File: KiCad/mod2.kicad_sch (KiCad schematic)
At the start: 47 parts, among them M3 Fan_4pin, M4 Fan_4pin, U2 ZD25Q64BSIGT

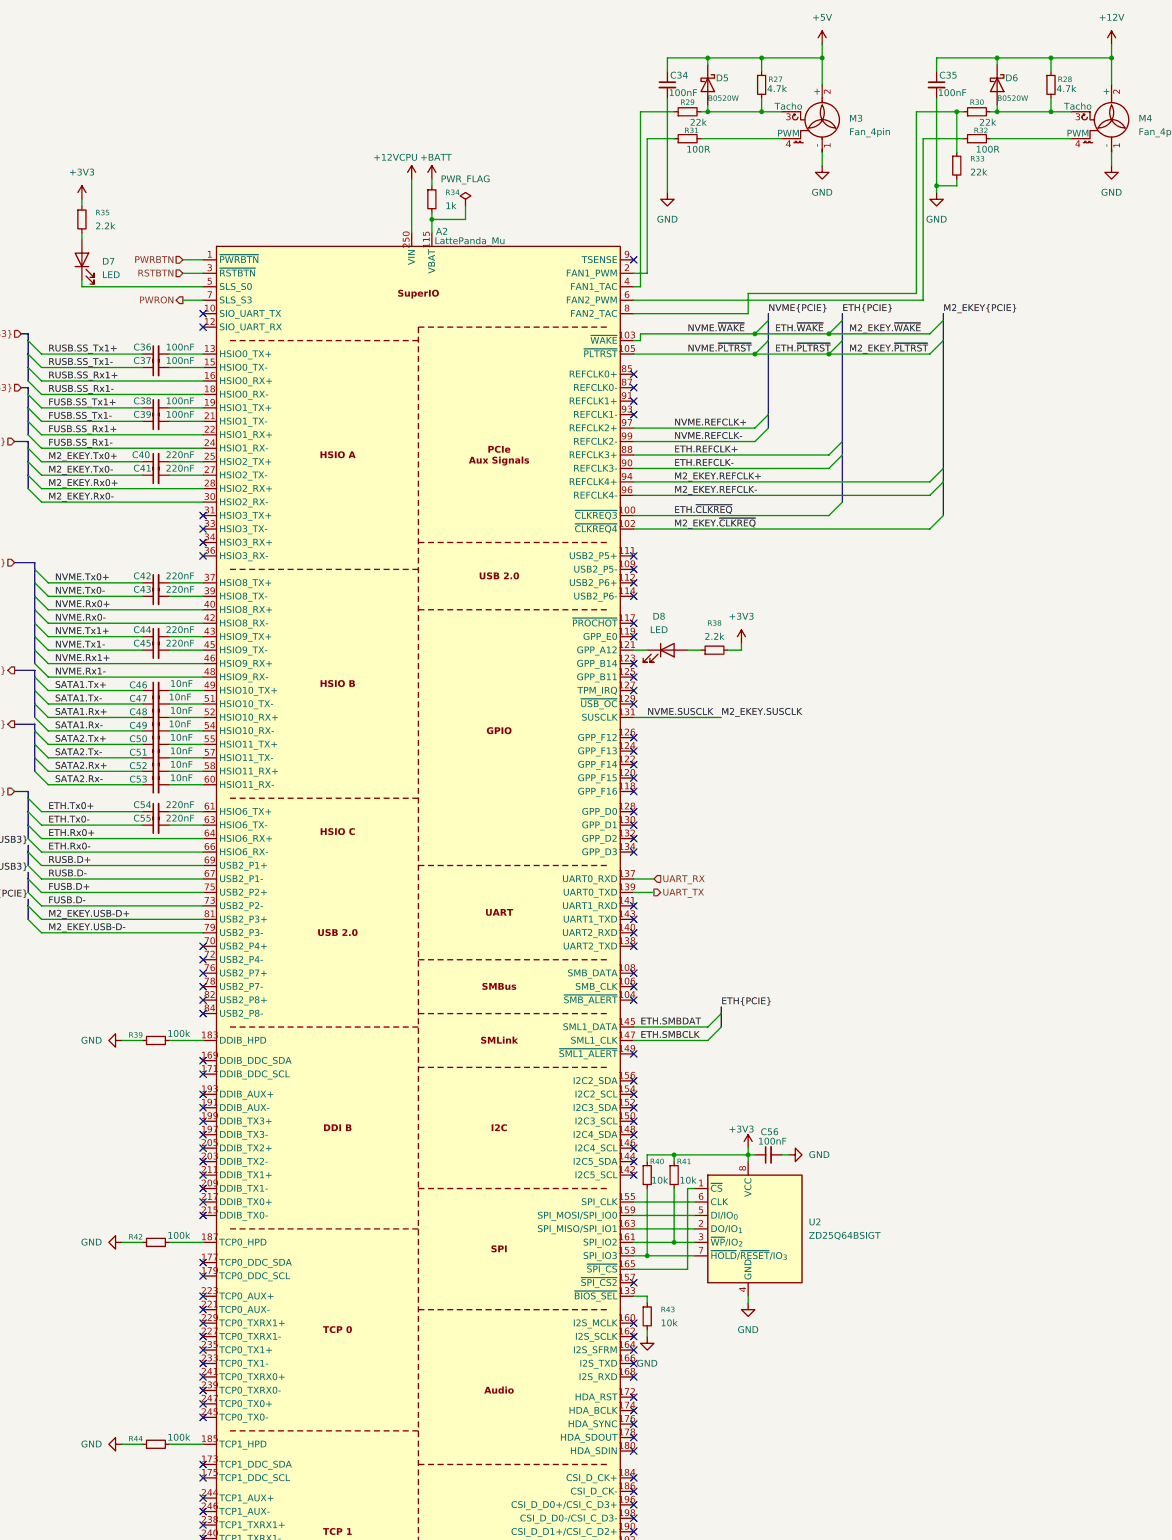
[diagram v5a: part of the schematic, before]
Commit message: Re-annotate schematic
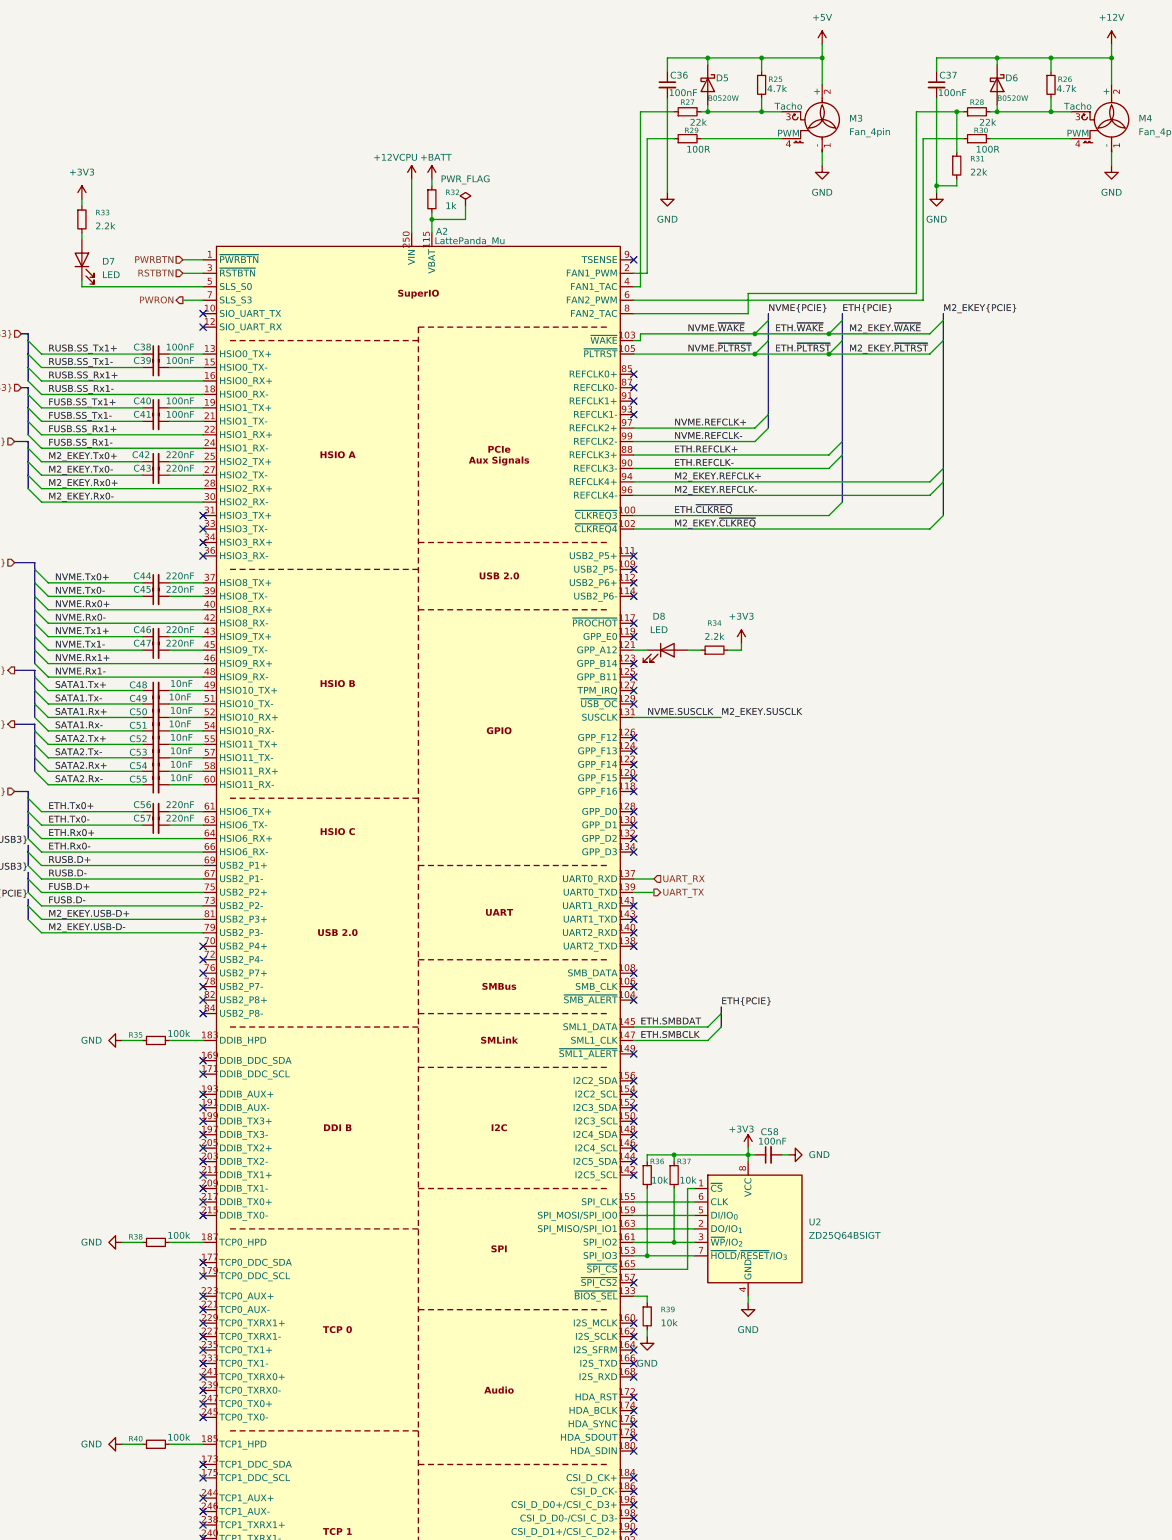
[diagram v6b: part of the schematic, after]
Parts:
- renumbered C34 to C36, C35 to C37, C36 to C38, C37 to C39, C38 to C40, C39 to C41, C40 to C42, C41 to C43, C42 to C44, C43 to C45, C44 to C46, C45 to C47, C46 to C48, C47 to C49, C48 to C50, C49 to C51, C50 to C52, C51 to C53, C52 to C54, C53 to C55, C54 to C56, C55 to C57, C56 to C58, R27 to R25, R28 to R26, R29 to R27, R30 to R28, R31 to R29, R32 to R30, R33 to R31, R34 to R32, R35 to R33, R38 to R34, R39 to R35, R40 to R36, R41 to R37, R42 to R38, R43 to R39, R44 to R40

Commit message: Get rid of extra sheets, make module sheets pretty
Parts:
- removed D5, D6: B0520W, Diode_SMD:D_SOD-123, symbol Device:D_Schottky
- removed D7, D8: LED, LED_SMD:LED_0603_1608Metric, symbol Device:LED
- removed M3: Fan_4pin, Connector_JST:JST_PH_B4B-PH-K_1x04_P2.00mm_Vertical, symbol Motor:Fan_4pin
- removed M4: Fan_4pin, Connector:FanPinHeader_1x04_P2.54mm_Vertical, symbol Motor:Fan_4pin
- removed U2: ZD25Q64BSIGT, Package_SO:SOIC-8_5.3x5.3mm_P1.27mm, symbol Memory_Flash:W25Q128JVS
- added C2, C24, C25, C26: 10uF, Capacitor_SMD:C_0603_1608Metric, symbol Device:C_Small
- added C231, C232, C358, C361: 2.2uF, Capacitor_SMD:C_0402_1005Metric, symbol Device:C_Small
- added C245: 220nF, Capacitor_SMD:C_0402_1005Metric, symbol Device:C_Small
- added C27, C28, C29, C30, C31, C32, C33, C34, C35, C357, C359, C363, C364, C366, C369, C371, C372, C373, C374, C375, C376, C377, C378: 100nF, Capacitor_SMD:C_0402_1005Metric, symbol Device:C_Small
- added C360: 10uF, Capacitor_SMD:C_0402_1005Metric, symbol Device:C_Small
- added C362: 1uF, Capacitor_SMD:C_0402_1005Metric, symbol Device:C_Small
- added C365, C368: 27pF, Capacitor_SMD:C_0402_1005Metric, symbol Device:C_Small
- added C367: 390pF, Capacitor_SMD:C_0402_1005Metric, symbol Device:C
- added C370: 100pF, Capacitor_SMD:C_0402_1005Metric, symbol Device:C_Small
- added D2, D8: B0520W, Diode_SMD:D_SOD-123, symbol Device:D_Schottky
- added D34, D5, D6: LED, LED_SMD:LED_0603_1608Metric, symbol Device:LED
- added H12, H13: MountingHole_Pad, MountingHole:MountingHole_2.2mm_M2_Pad_Via, symbol Mechanical:MountingHole_Pad
- added J19: RJ45_LED_Shielded_x2, symbol Connector:RJ45_LED_Shielded_x2
- added J26: USB3_A, symbol Connector:USB3_A
- added J28: Bus_M.2_Socket_M, EasyEDA2KiCAD:CONN-SMD_AS0BC21-S30BM-7H, symbol Connector:Bus_M.2_Socket_M
- added J29: Bus_M.2_Socket_E, EasyEDA2KiCAD:CONN-SMD_AS0BC21-S48BE-7H, symbol Connector:Bus_M.2_Socket_E
- added J32: HDMI_A, Connector_Video:HDMI_A_Molex_208658-1001_Horizontal, symbol Connector:HDMI_A
- added J4: USB3_IDC, Connector_IDC:IDC-Header_2x10_P2.54mm_Vertical, symbol Custom:USB3_IDC
- added J5: SFF-8087, symbol Custom:SFF-8087
- added M2: Fan_4pin, Connector_JST:JST_PH_B4B-PH-K_1x04_P2.00mm_Vertical, symbol Motor:Fan_4pin
- added Q5, Q6, Q7, Q8: 2N7002, Package_TO_SOT_SMD:SOT-23, symbol Transistor_FET:Q_NMOS_GSD
- added R10: 4.7k, Resistor_SMD:R_0402_1005Metric, symbol Device:R_Small
- added R11, R237: 22k, Resistor_SMD:R_0402_1005Metric, symbol Device:R_Small
- added R110, R215: 75R, Resistor_SMD:R_0402_1005Metric, symbol Device:R_Small
- added R13: 100R, Resistor_SMD:R_0402_1005Metric, symbol Device:R_Small
- added R14, R18, R231, R232, R234, R235: 2.2k, Resistor_SMD:R_0402_1005Metric, symbol Device:R_Small
- added R15, R236: 1k, Resistor_SMD:R_0805_2012Metric, symbol Device:R_Small
- added R16, R17, R216, R217, R221: 10k, Resistor_SMD:R_0402_1005Metric, symbol Device:R_Small
- added R218: 2.49k, Resistor_SMD:R_0402_1005Metric, symbol Device:R_Small
- added R219: 510R, Resistor_SMD:R_0402_1005Metric, symbol Device:R_Small
- added R220, R222: 100k, Resistor_SMD:R_0402_1005Metric, symbol Device:R_Small
- added R223, R224, R225, R226, R227, R228, R229, R230: 470R, Resistor_SMD:R_0402_1005Metric, symbol Device:R_Small
- added R233: 1M, Resistor_SMD:R_0402_1005Metric, symbol Device:R_Small
- added TR6: QG2439S, Custom:QG2439S, symbol Transformer:30F-51NL
- added U2, U46, U50, U51, U52: H5VU25U, Package_DFN_QFN:Diodes_UDFN-10_1.0x2.5mm_P0.5mm, symbol Power_Protection:D3V3XA4B10LP
- added U47: RTL8125BG-CG, Package_DFN_QFN:QFN-48-1EP_6x6mm_P0.4mm_EP4.2x4.2mm, symbol Custom:RTL8125BG-CG
- added U48: ZD25Q64BSIGT, Package_SO:SOIC-8_5.3x5.3mm_P1.27mm, symbol Memory_Flash:W25Q128JVS
- added U49: M24C02-WMN, Package_SO:SOIC-8_3.9x4.9mm_P1.27mm, symbol Memory_EEPROM:M24C02-WMN
- added Y7: 25MHz, Crystal:Crystal_SMD_3225-4Pin_3.2x2.5mm, symbol Device:Crystal_GND24
- C36, C37, C38, C39, C40, C41, C58: value 100nF -> 220nF
- C42, C43, C44, C45, C46, C47: value 220nF -> 10nF
- C48: value 10nF -> 1uF
- C49, C54: value 10nF -> 2.2uF
- C51, C52, C55: value 10nF -> 10uF
- C56, C57: value 220nF -> 2.2uF
- R25, R26: value 4.7k -> 100R
- R27, R28, R31: value 22k -> 4.7k
- R29, R30: value 100R -> 4.7k
- R32: value 1k -> 100R; footprint Resistor_SMD:R_0805_2012Metric -> Resistor_SMD:R_0402_1005Metric
- R33: value 2.2k -> 100R
- R34: value 2.2k -> 510R
- R35, R38: value 100k -> 4.7k
- R36: value 10k -> 4.7k
- R37: value 10k -> 510R
- R39: value 10k -> 75R
- R40: value 100k -> 75R
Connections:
- net FUSB.SS_Tx1+ is gone; now on net NVME.Tx1+: C40.1
- net FUSB.SS_Tx1- is gone; now on net NVME.Tx1-: C41.1
- net RUSB.SS_Tx1+ is gone; now on net NVME.Tx0+: C38.1
- net RUSB.SS_Tx1- is gone; now on net NVME.Tx0-: C39.1
- net SATA1.Rx- is gone; now on net GND: C51.1
- net SATA1.Tx+ is gone; now on net GND: C48.1
- net SATA2.Rx+ is gone; now on net GND: C54.1
- net SATA2.Rx- is gone; now on net +0V95: C55.1
- net SATA2.Tx+ is gone; now on net +0V95: C52.1
- net UART_TX is gone; now on an unnamed net: A2.139 (UART0_TXD)
- net +3V3: now also C2.1, C24.1, C25.1, C26.1, C27.1, C28.1, C29.1, C30.1, C366.1, J28.12 (3.3V), J28.14 (3.3V), J28.16 (3.3V), J28.18 (3.3V), J28.2 (3.3V), J28.4 (3.3V), J28.70 (3.3V), J28.72 (3.3V), J28.74 (3.3V), J29.2 (3.3V), J29.4 (3.3V), J29.72 (3.3V), J29.74 (3.3V), Q6.1 (G), Q7.1 (G), Q8.1 (G), R14.1, R16.2, R17.2, R18.2, R216.1, R217.1, R219.2, R233.1, R234.1, R235.1, U48.8 (VCC); no longer C58.1, R33.1, R34.2, R36.1, R37.1
- net +5V: now also C31.1, D2.1 (K), J26.1 (VBUS), J4.11 (VBUS2), M2.2 (+), R10.1; no longer C36.1, R25.1
- net +BATT: now also R15.1; no longer R32.1
- net ETH.REFCLK+: now also A2.94 (REFCLK4+), U47.44 (REFCLK_P); no longer A2.88 (REFCLK3+)
- net ETH.REFCLK-: now also A2.96 (REFCLK4-), U47.45 (REFCLK_N); no longer A2.90 (REFCLK3-)
- net ETH.Rx0+: now also C363.1
- net ETH.Rx0-: now also C364.1
- net ETH.Tx0+: now also C58.1, U47.41 (HSIP); no longer C56.1
- net ETH.Tx0-: now also C245.1, U47.42 (HSIN); no longer C57.1
- net ETH.~{CLKREQ}: now also A2.102 (~{CLKREQ4}), R36.2, U47.48 (CLKREQB); no longer A2.100 (~{CLKREQ3})
- net ETH.~{PLTRST}: now also J28.50 (~{PERST}), J29.52 (~{PERST0}), U47.36 (~{PERRST})
- net ETH.~{WAKE}: now also R35.2, J28.54 (~{PEWAKE}), J29.55 (~{PEWAKE0}), U47.2 (LANWAKEB)
- net GND: now also C49.2, C52.2, C55.2, C56.1, C57.2, R38.2, C2.2, C231.1, C232.2, C24.2, C25.2, C26.2, C27.2, C28.2, C29.2, C30.2, C31.2, C357.1, C358.2, C359.1, C360.2, C361.1, C362.2, C365.1, C366.2, C367.1, C368.1, C369.1, C370.2, H12.1, H13.1, J19.SH, J26.10 (SHIELD), J26.4 (GND), J26.7 (DRAIN), J28.1 (GND), J28.15 (GND), J28.21 (GND), J28.27 (GND), J28.3 (GND), J28.33 (GND), J28.39 (GND), J28.45 (GND), J28.51 (GND), J28.57 (GND), J28.71 (GND), J28.73 (GND), J28.75 (GND), J28.9 (GND), J28.MP, J29.1 (GND), J29.18 (GND), J29.33 (GND), J29.39 (GND), J29.45 (GND), J29.51 (GND), J29.57 (GND), J29.63 (GND), J29.69 (GND), J29.7 (GND), J29.75 (GND), J29.MP, J32.11 (CKS), J32.17 (GND), J32.2 (D2S), J32.5 (D1S), J32.8 (D0S), J32.SH, J4.14 (GND2), J4.17 (DRAIN2), J5.A12 (GND), J5.A15 (GND), J5.A18 (GND), J5.B12 (GND), J5.B15 (GND), J5.B18 (GND), M2.1 (-), Q5.2 (S), R218.2, R220.1, R221.2, R222.1, R223.2, R224.2, R225.2, R226.2, R227.2, R228.2, R229.2, R230.2, R237.2, U2.3 (VSS), U2.8 (VSS), U46.3 (VSS), U46.8 (VSS), U47.40 (GND), U47.49 (GND), U48.4 (GND), U49.1 (E0), U49.2 (E1), U49.3 (E2), U49.4 (VSS), U49.7 (~{WC}), U50.3 (VSS), U50.8 (VSS), U51.3 (VSS), U51.8 (VSS), U52.3 (VSS), U52.8 (VSS), Y7.2, Y7.4; no longer C36.2, C37.2, C58.2, R31.2, R35.1, R38.1, R39.2, R40.1
- net M2_EKEY.REFCLK+: now also A2.88 (REFCLK3+), J29.47 (REFCLKp0); no longer A2.94 (REFCLK4+)
- net M2_EKEY.REFCLK-: now also A2.90 (REFCLK3-), J29.49 (REFCLKn0); no longer A2.96 (REFCLK4-)
- net M2_EKEY.Rx0+: now also J29.41 (PERp0)
- net M2_EKEY.Rx0-: now also J29.43 (PERn0)
- net M2_EKEY.SUSCLK: now also J28.68 (SUSCLK), J29.50 (SUSCLK)
- net M2_EKEY.Tx0+: now also C36.1, J29.35 (PETp0); no longer C42.1
- net M2_EKEY.Tx0-: now also C37.1, J29.37 (PETn0); no longer C43.1
- net M2_EKEY.USB-D+: now also J29.3 (USB_D+)
- net M2_EKEY.USB-D-: now also J29.5 (USB_D-)
- net M2_EKEY.~{CLKREQ}: now also A2.100 (~{CLKREQ3}), J29.53 (~{CLKREQ0}); no longer A2.102 (~{CLKREQ4})
- net NVME.REFCLK+: now also A2.91 (REFCLK1+), J28.55 (REFCLKp); no longer A2.97 (REFCLK2+)
- net NVME.REFCLK-: now also A2.93 (REFCLK1-), J28.53 (REFCLKn); no longer A2.99 (REFCLK2-)
- net NVME.Rx0+: now also J28.43 (PERp0/SATA-B-)
- net NVME.Rx0-: now also J28.41 (PERn0/SATA-B+)
- net NVME.Rx1+: now also J28.31 (PERp1)
- net NVME.Rx1-: now also J28.29 (PERn1)
- net NVME.Tx0+: now also J28.49 (PETp0/SATA-A+); no longer C44.1
- net NVME.Tx0-: now also J28.47 (PETn0/SATA-A-); no longer C45.1
- net NVME.Tx1+: now also J28.37 (PETp1); no longer C46.1
- net NVME.Tx1-: now also J28.35 (PETn1); no longer C47.1
- net at A2.55 (HSIO11_TX+): now also C46.2; no longer C52.2
- net at C47.2: now also A2.57 (HSIO11_TX-); no longer A2.45 (HSIO9_TX-)
- net at A2.63 (HSIO6_TX-): now also C245.2; no longer C57.2
- net at A2.52 (HSIO10_RX+): now also C44.2; no longer C50.2
- net at A2.2 (FAN1_PWM): now also R13.1; no longer R29.1
- net at R29.2: now also U47.31 (EECS/SCL), U49.6 (SCL)
- net at A2.115 (VBAT): now also R15.2; no longer R32.2
- net at A2.13 (HSIO0_TX+): now also C32.2; no longer C38.2
- net at R39.1: now also TR6.24 (CT); no longer A2.133 (~{BIOS_SEL})
- net at A2.141 (UART1_RXD): now also R32.1
- net at A2.143 (UART1_TXD): now also R33.1
- net at C39.2: now also A2.39 (HSIO8_TX-); no longer A2.15 (HSIO0_TX-)
- net at A2.153 (SPI_IO3): now also R217.2, U48.7 (~{HOLD}/~{RESET}/IO_{3}); no longer R36.2
- net at A2.155 (SPI_CLK): now also U48.6 (CLK)
- net at A2.159 (SPI_MOSI/SPI_IO0): now also U48.5 (DI/IO_{0})
- net at A2.161 (SPI_IO2): now also R216.2, U48.3 (~{WP}/IO_{2}); no longer R37.2
- net at A2.163 (SPI_MISO/SPI_IO1): now also U48.2 (DO/IO_{1})
- net at A2.165 (~{SPI_CS}): now also U48.1 (~{CS})
- net REAR_DISPLAY.SDA: now reaches A2.169 (DDIB_DDC_SDA)
- net REAR_DISPLAY.SDA: now also Q7.2 (S), R234.2
- net REAR_DISPLAY.SCL: now reaches A2.171 (DDIB_DDC_SCL)
- net REAR_DISPLAY.SCL: now also Q6.2 (S), R235.2
- net REAR_DISPLAY.HPD: now reaches A2.183 (DDIB_HPD)
- net REAR_DISPLAY.HPD: now also Q8.2 (S), R233.2; no longer R35.2
- net at R40.2: now also R39.2, C370.1, R110.2, R215.2; no longer A2.185 (TCP1_HPD)
- net at A2.187 (TCP0_HPD): now also R220.2; no longer R38.2
- net at A2.19 (HSIO1_TX+): now also C34.2; no longer C40.2
- net REAR_DISPLAY.Tx3-: now reaches A2.197 (DDIB_TX3-)
- net REAR_DISPLAY.Tx3-: now also C378.1
- net REAR_DISPLAY.Tx3+: now reaches A2.199 (DDIB_TX3+)
- net REAR_DISPLAY.Tx3+: now also C377.1
- net REAR_DISPLAY.Tx2-: now reaches A2.203 (DDIB_TX2-)
- net REAR_DISPLAY.Tx2-: now also C376.1
- net REAR_DISPLAY.Tx2+: now reaches A2.205 (DDIB_TX2+)
- net REAR_DISPLAY.Tx2+: now also C375.1
- net REAR_DISPLAY.Tx1-: now reaches A2.209 (DDIB_TX1-)
- net REAR_DISPLAY.Tx1-: now also C374.1
- net at C41.2: now also A2.45 (HSIO9_TX-); no longer A2.21 (HSIO1_TX-)
- net REAR_DISPLAY.Tx1+: now reaches A2.211 (DDIB_TX1+)
- net REAR_DISPLAY.Tx1+: now also C373.1
- net REAR_DISPLAY.Tx0-: now reaches A2.215 (DDIB_TX0-)
- net REAR_DISPLAY.Tx0-: now also C372.1
- net REAR_DISPLAY.Tx0+: now reaches A2.217 (DDIB_TX0+)
- net REAR_DISPLAY.Tx0+: now also C371.1
- net at C42.2: now also A2.49 (HSIO10_TX+); no longer A2.25 (HSIO2_TX+)
- net at C43.2: now also A2.51 (HSIO10_TX-); no longer A2.27 (HSIO2_TX-)
- net at A2.37 (HSIO8_TX+): now also C38.2; no longer C44.2
- net at C45.2: now also A2.54 (HSIO10_RX-); no longer A2.39 (HSIO8_TX-)
- net at A2.4 (FAN1_TAC): now also R11.1; no longer R27.1
- net at A2.43 (HSIO9_TX+): now also C40.2; no longer C46.2
- net +3V3SB: now reaches C48.2
- net +3V3SB: now also C51.2, C54.2, C56.2, R27.1, R28.1, R29.1, R30.1, R31.1, R34.2, R35.1, R36.1, R37.2, C231.2, C357.2, C359.2, C361.2, C369.2, U47.15 (AVDD33), U47.19 (AVDD33), U47.29 (DVDD33), U47.33 (AVDD33), U47.34 (AVDD33_XTAL), U47.43 (EVDD33), U47.46 (DVDD33), U49.8 (VCC); no longer A2.49 (HSIO10_TX+)
- net SLS_S0: now reaches A2.5 (SLS_S0)
- net SLS_S0: now also R38.1, Q5.1 (G), U47.1 (~{ISOLATEB})
- net at C53.2: now also A2.60 (HSIO11_RX-); no longer A2.57 (HSIO11_TX-)
- net at A2.58 (HSIO11_RX+): now also C50.2; no longer C54.2
- net at A2.6 (FAN2_PWM): no longer R30.1
- net at A2.61 (HSIO6_TX+): now also C58.2; no longer C56.2
- net SLOT1_UART_TX: now reaches R33.2
- net at R34.1: now also J19.24
- net at R27.2: now also U47.32 (EEPROM_SEL); no longer R25.2
- net at R28.2: now also U47.3 (GPI); no longer R26.2
- net at R30.2: now also U47.30 (EEDI/SDA), U49.5 (SDA)
- net +12V: no longer names the net of R26.1
- net +12V: no longer C37.1
- net ETH.SMBCLK: no longer names the net of A2.147 (SML1_CLK)
- net ETH.SMBDAT: no longer names the net of A2.145 (SML1_DATA)
- net FUSB.D+ renamed USB1_D+
- net USB1_D+: now also J4.13 (D2+)
- net FUSB.D- renamed USB1_D-
- net USB1_D-: now also J4.12 (D2-)
- net FUSB.SS_Rx1+: no longer names the net of A2.22 (HSIO1_RX+)
- net FUSB.SS_Rx1+: now also J4.16 (SSRX2+)
- net FUSB.SS_Rx1-: no longer names the net of A2.24 (HSIO1_RX-)
- net FUSB.SS_Rx1-: now also J4.15 (SSRX2-)
- net RUSB.D+ renamed USB0_D+
- net USB0_D+: now also J26.3 (D+)
- net RUSB.D- renamed USB0_D-
- net USB0_D-: now also J26.2 (D-)
- net RUSB.SS_Rx1+: no longer names the net of A2.16 (HSIO0_RX+)
- net RUSB.SS_Rx1+: now also J26.6 (SSRX+)
- net RUSB.SS_Rx1-: no longer names the net of A2.18 (HSIO0_RX-)
- net RUSB.SS_Rx1-: now also J26.5 (SSRX-)
- net SATA1.Rx+: no longer names the net of C50.1
- net SATA1.Rx+: now also J5.A16 (Rx3+)
- net SATA1.Tx- renamed +0V95
- net +0V95: now also C57.1, C232.1, C358.1, C360.1, C362.1, U47.11 (AVDD09), U47.16 (AVDD09), U47.22 (AVDD09), U47.28 (DVDD09), U47.37 (EVDD09), U47.47 (DVDD09), U47.8 (DVDD09)
- net SATA2.Tx-: no longer names the net of C53.1
- net SATA2.Tx-: now also J5.A17 (Rx3-)
- net UART_RX: no longer names the net of A2.137 (UART0_RXD)
- net UART_RX: now also R25.1
- new net: C42.1, J5.B13 (Tx2+)
- new net: C43.1, J5.B14 (Tx2-)
- new net: A2.25 (HSIO2_TX+), C36.2
- new net: J19.22, R37.1
- new net: C34.1, J4.19 (SSTX2+)
- new net: D5.1 (K), Q5.3 (D)
- new net: J29.54 (~{W_DISABLE2}), R17.1
- new net: J29.56 (~{W_DISABLE1}), R16.1
- new net: R110.1, TR6.18 (CT)
- new net: C44.1, J5.A13 (Rx2+)
- new net: D2.2 (A), M2.3 (Tacho), R10.2, R11.2
- new net: M2.4 (PWM), R13.2
- new net: D8.2 (A), U47.6 (POW_EXT_SWR)
- new net: R215.1, TR6.15 (CT)
- new net: Q8.3 (D), R236.1, R237.1
- new net: D6.2 (A), R18.1
- new net: A2.133 (~{BIOS_SEL}), R221.1
- new net: C33.1, J26.8 (SSTX-)
- new net: C32.1, J26.9 (SSTX+)
- new net: C45.1, J5.A14 (Rx2-)
- new net: D5.2 (A), R14.2
- new net: C46.1, J5.B16 (Tx3+)
- new net: C365.2, U47.10 (CKXTAL1), Y7.1
- new net: C368.2, U47.9 (CKXTAL2), Y7.3
- new net: C47.1, J5.B17 (Tx3-)
- new net: R218.1, U47.12 (RSET)
- new net: D6.1 (K), J28.10 (DAS/~{DSS}/~{LED1})
- new net: D34.1 (K), U47.35 (LED3)
- new net: D34.2 (A), R219.1
- new net: C364.2, U47.39 (HSON)
- new net: R40.1, TR6.21 (CT)
- new net: C367.2, TR6.1 (CT), TR6.10 (CT), TR6.4 (CT), TR6.7 (CT)
- new net: A2.15 (HSIO0_TX-), C33.2
- new net: C363.2, U47.38 (HSOP)
- new net: J19.21, U47.25 (EEDO)
- new net: J19.23, R31.2, U47.27 (EESK)
- new net: U47.4 (NC), U47.5 (NC), U47.7 (NC)
- new net: C35.1, J4.18 (SSTX2-)
- new net: J19.13, TR6.13 (MX4-)
- new net: J19.14, TR6.14 (MX4+)
- new net: J19.15, TR6.16 (MX3-)
- new net: J19.18, TR6.17 (MX3+)
- new net: J19.16, TR6.19 (MX2-)
- new net: J19.17, TR6.20 (MX2+)
- new net: J19.19, TR6.22 (MX1-)
- new net: J19.20, TR6.23 (MX1+)
- new net: A2.27 (HSIO2_TX-), C37.2
- new net: A2.185 (TCP1_HPD), R222.2
- new net: A2.21 (HSIO1_TX-), C35.2
- new net +5VHDMI: J32.18 (+5V), R231.1, R232.1
- new net 0V95_EN: D8.1 (K)
- new net HDMI_CK+: C377.2, J32.10 (CK+), R229.1, U51.4, U51.7 (NC)
- new net HDMI_CK-: C378.2, J32.12 (CK-), R230.1, U51.5, U51.6 (NC)
- new net HDMI_D0+: C375.2, J32.7 (D0+), R227.1, U51.1, U51.10 (NC)
- new net HDMI_D0-: C376.2, J32.9 (D0-), R228.1, U51.2, U51.9 (NC)
- new net HDMI_D1+: C373.2, J32.4 (D1+), R225.1, U50.4, U50.7 (NC)
- new net HDMI_D1-: C374.2, J32.6 (D1-), R226.1, U50.5, U50.6 (NC)
- new net HDMI_D2+: C371.2, J32.1 (D2+), R223.1, U50.1, U50.10 (NC)
- new net HDMI_D2-: C372.2, J32.3 (D2-), R224.1, U50.2, U50.9 (NC)
- new net HDMI_HPD: J32.19 (HPD), R236.2, U52.4, U52.7 (NC)
- new net HDMI_SCL: J32.15 (SCL), Q6.3 (D), R231.2, U52.1, U52.10 (NC)
- new net HDMI_SDA: J32.16 (SDA), Q7.3 (D), R232.2, U52.2, U52.9 (NC)
- new net MDI0+: TR6.12 (TD4-), U2.1, U2.10 (NC), U47.13 (MDIP0)
- new net MDI0-: TR6.11 (TD4+), U2.2, U2.9 (NC), U47.14 (MDIN0)
- new net MDI1+: TR6.9 (TD3-), U2.4, U2.7 (NC), U47.17 (MDIP1)
- new net MDI1-: TR6.8 (TD3+), U2.5, U2.6 (NC), U47.18 (MDIN1)
- new net MDI2+: TR6.6 (TD2-), U46.1, U46.10 (NC), U47.20 (MDIP2)
- new net MDI2-: TR6.5 (TD2+), U46.2, U46.9 (NC), U47.21 (MDIN2)
- new net MDI3+: TR6.3 (TD1-), U46.4, U46.7 (NC), U47.23 (MDIP3)
- new net MDI3-: TR6.2 (TD1+), U46.5, U46.6 (NC), U47.24 (MDIN3)
- new net PCIE_UART_RX: R25.2
- new net PCIE_UART_TX: R26.2
- new net SLOT1_UART_RX: R32.2
- now unconnected: A2.8 (FAN2_TAC)
- no-connect marks 111 -> 152
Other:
- note added: "2.5G Ethernet"
- note added: "LattePanda Mu SODIMM Socket"
- note added: "M.2 E-Key"
- note added: "M.2 NVME"
- note added: "Micro HDMI"
- note added: "SATA"
- note added: "USB3"
